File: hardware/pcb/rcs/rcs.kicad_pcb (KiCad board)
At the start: 2 copper layers, 160.5 x 112 mm, 19 parts, among them J1 Conn_01x02_Socket, J2 Conn_01x02_Socket, J3 Conn_01x02_Socket, J4 Conn_01x02_Socket, J5 Conn_01x02_Socket, J6 Conn_01x02_Socket, Q1 BS170, Q2 BS170, Q3 BS170, Q4 BS170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

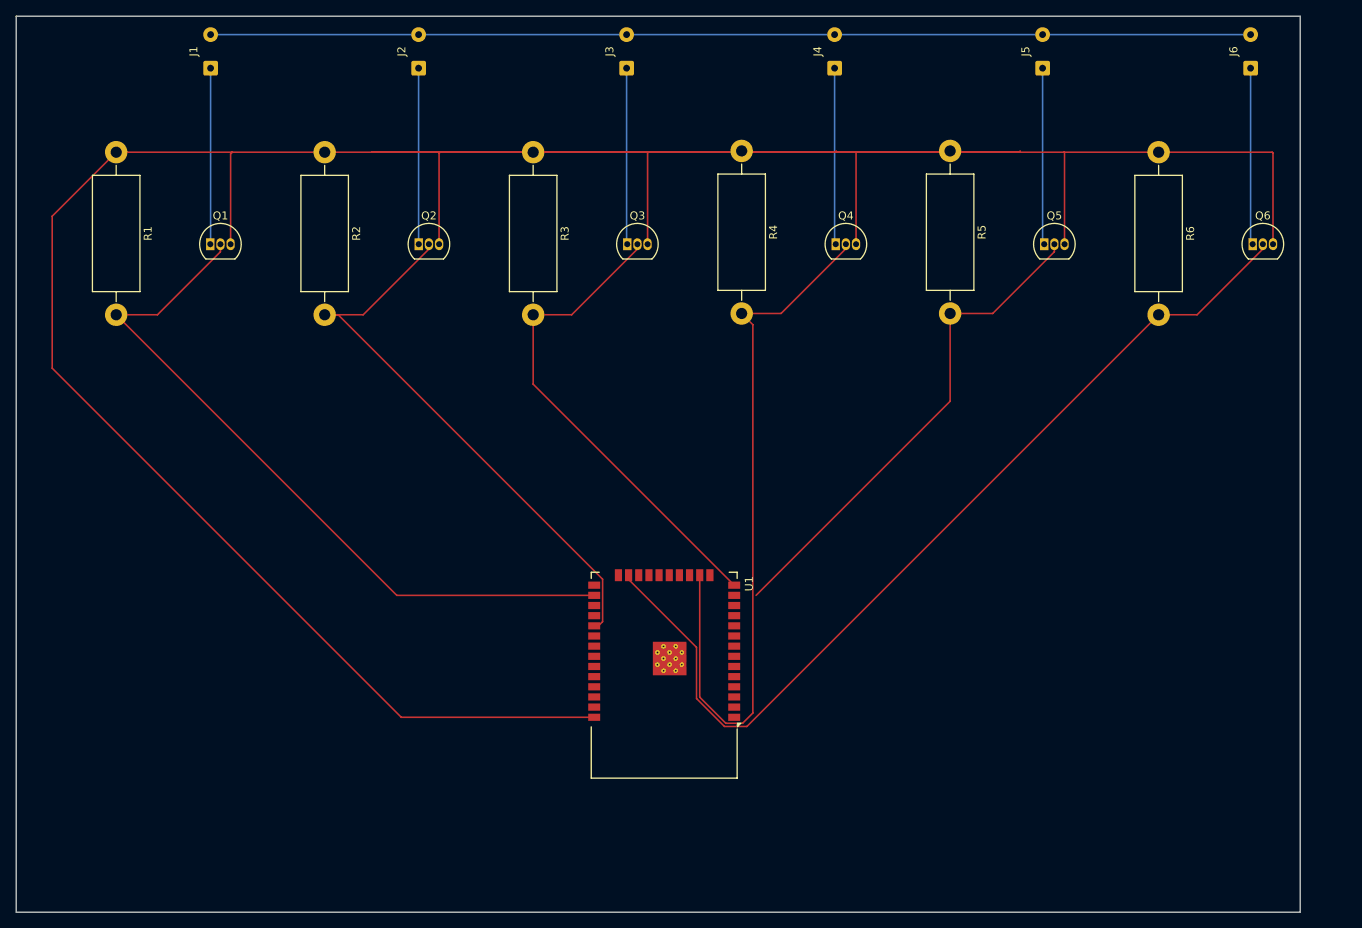
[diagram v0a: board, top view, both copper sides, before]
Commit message: Add ESP32 dev board schematic and footprint, make draft PCB
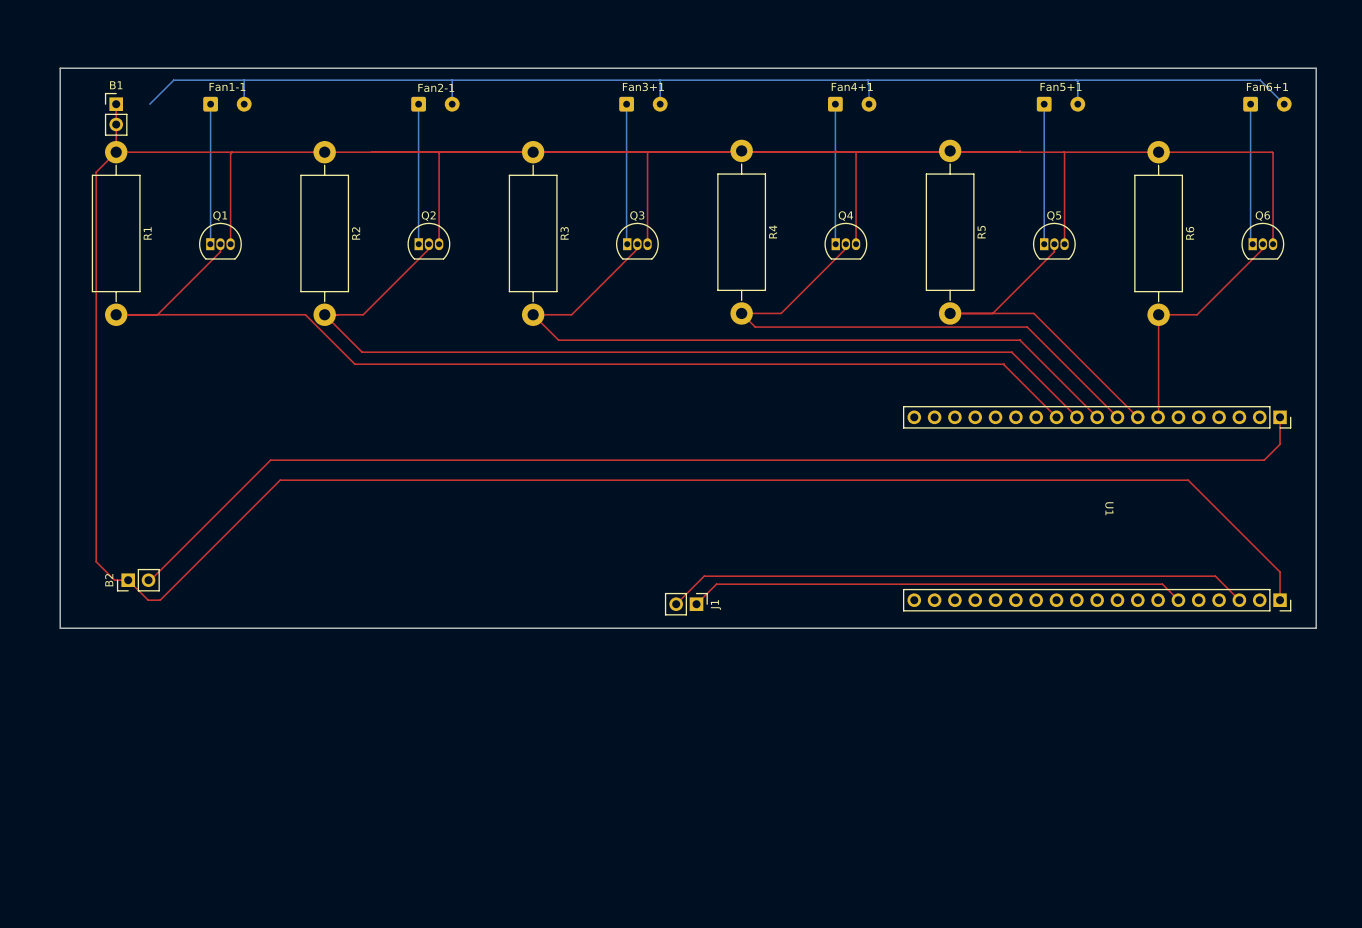
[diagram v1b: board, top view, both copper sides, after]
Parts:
- added B1: 4S, Connector_PinHeader_2.54mm:PinHeader_1x02_P2.54mm_Vertical, F.Cu at (74.0, 24.0)
- added B2: 3V3, Connector_PinHeader_2.54mm:PinHeader_1x02_P2.54mm_Vertical, F.Cu at (75.5, 83.5)
- added J1: UART, Connector_PinHeader_2.54mm:PinHeader_1x02_P2.54mm_Vertical, F.Cu at (146.5, 86.5)
- Fan1-1: renamed from J1; value Conn_01x02_Socket -> Fan1+
- Fan2-1: renamed from J2; value Conn_01x02_Socket -> Fan2+
- Fan3+1: renamed from J3; value Conn_01x02_Socket -> Fan3-
- Fan4+1: renamed from J4; value Conn_01x02_Socket -> Fan4-
- Fan5+1: renamed from J5; value Conn_01x02_Socket -> Fan5-
- Fan6+1: renamed from J6; value Conn_01x02_Socket -> Fan6-
- U1: value ESP32-WROOM-32 -> ESP32; footprint RF_Module:ESP32-WROOM-32 -> custom:ESP32
- moved U1 79.0 mm to (219.5, 74.6), turned to -90 degrees
- moved Fan5+1 4.50 mm to (190.0, 24.0), turned to 0 degrees
- moved Fan4+1 4.50 mm to (163.9, 24.0), turned to 0 degrees
- moved Fan1-1 4.50 mm to (85.8, 24.0), turned to 0 degrees
- moved Fan2-1 4.50 mm to (111.8, 24.0), turned to 0 degrees
- moved Fan3+1 4.50 mm to (137.8, 24.0), turned to 0 degrees
- moved Fan6+1 4.50 mm to (215.8, 24.0), turned to 0 degrees
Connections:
- U1 pad 1: GND -> +3.3V
- U1 pad 10: unconnected-(U1-IO25-Pad10) -> Fan3
- U1 pad 11: unconnected-(U1-IO26-Pad11) -> Fan2
- U1 pad 12: unconnected-(U1-IO27-Pad12) -> Fan1
- U1 pad 13: Fan5 -> unconnected-(U1-P12-Pad13)
- U1 pad 14: Fan3 -> unconnected-(U1-GND-Pad14)
- U1 pad 15: GND -> unconnected-(U1-P13-Pad15)
- U1 pad 16: Fan4 -> unconnected-(U1-SD2-Pad16)
- U1 pad 2: +3.3V -> unconnected-(U1-EN-Pad2)
- U1 pad 20: unconnected-(U1-SCK/CLK-Pad20) -> GND
- U1 pad 22: unconnected-(U1-SDI/SD1-Pad22) -> Net-(J1-Pin_2)
- U1 pad 23: Fan6 -> unconnected-(U1-TX-Pad23)
- U1 pad 25: unconnected-(U1-IO0-Pad25) -> Net-(J1-Pin_1)
- U1 pad 26: Fan1 -> unconnected-(U1-GND-Pad26)
- U1 pad 29: Fan2 -> unconnected-(U1-P18-Pad29)
- U1 pad 38: GND -> unconnected-(U1-CLK-Pad38)
- U1 pad 7: unconnected-(U1-IO35-Pad7) -> Fan6
- U1 pad 8: unconnected-(U1-IO32-Pad8) -> Fan5
- U1 pad 9: unconnected-(U1-IO33-Pad9) -> Fan4
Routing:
- net +3.3V: track 0.00 -> 152.0 mm
- net GND: track 469.1 -> 575.6 mm
- net Fan6: track 116.5 -> 29.9 mm
- net Net-(J1-Pin_2): track 0.00 -> 73.1 mm
- net Net-(J1-Pin_1): track 0.00 -> 62.1 mm
- net Fan1: track 91.5 -> 140.1 mm
- net Fan2: track 72.0 -> 118.1 mm
- net Fan3: track 61.3 -> 92.9 mm
- net +15V: track 130.0 -> 159.4 mm
- net Fan4: track 91.2 -> 69.3 mm
- net Fan5: track 62.5 -> 46.0 mm
- net Net-(Fan6+1-Pin_1): track 22.1 -> 17.6 mm
- net Net-(Fan3+1-Pin_1): track 22.0 -> 17.5 mm
- net Net-(Fan2-1-Pin_1): track 22.0 -> 17.5 mm
- net Net-(Fan1-1-Pin_1): track 22.0 -> 17.5 mm
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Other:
- board size 160.5 x 112 mm -> 157 x 70 mm

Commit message: More compact PCB layout
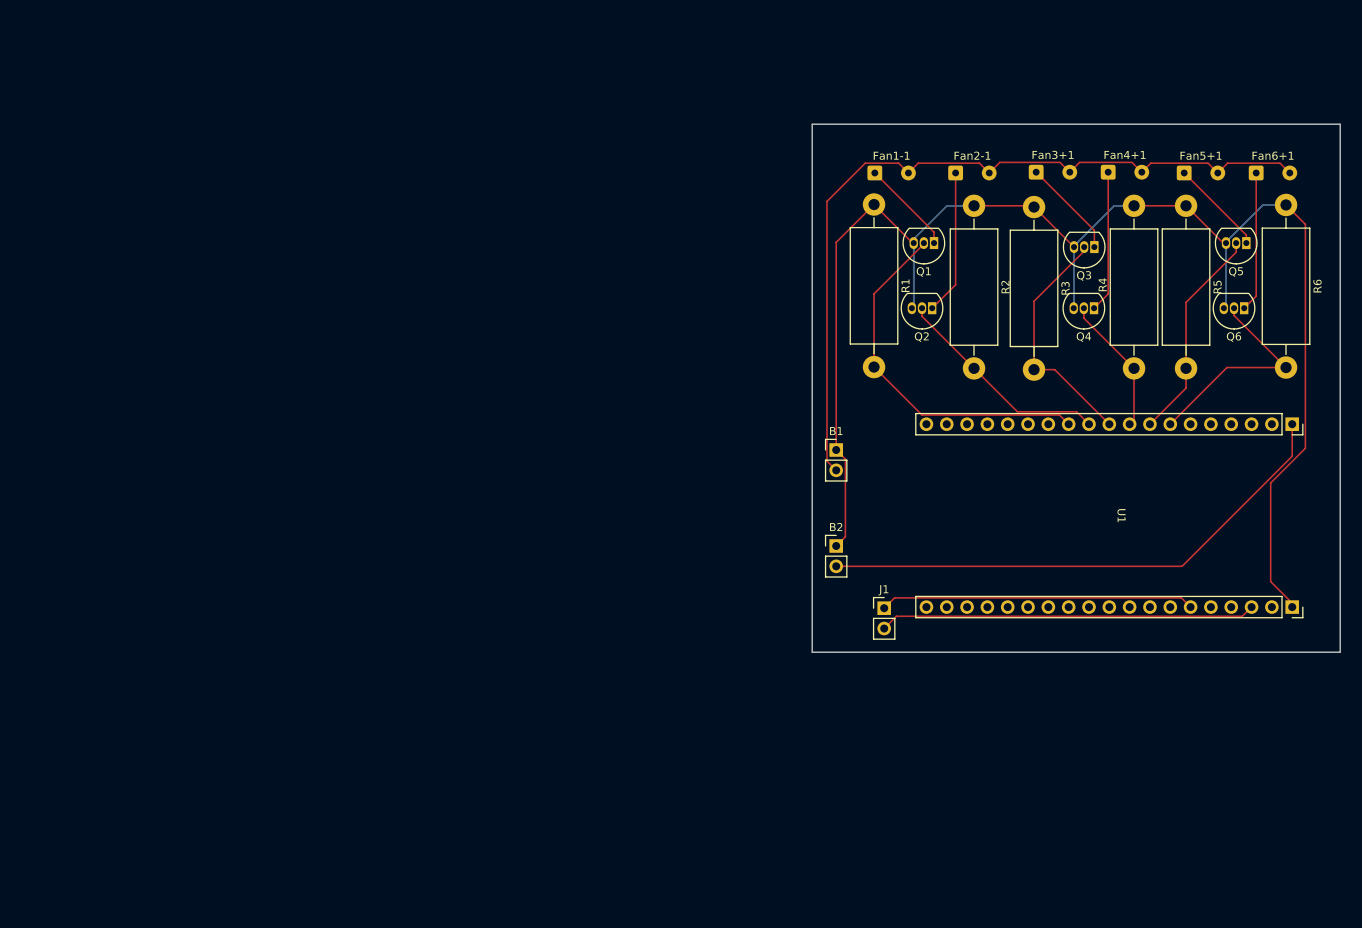
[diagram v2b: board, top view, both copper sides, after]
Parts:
- moved B1 99.8 mm to (164.0, 67.2)
- moved R1 95.0 mm to (168.7, 36.5)
- moved Q1 90.5 mm to (176.2, 41.4), turned to 180 degrees
- moved B2 88.6 mm to (164.0, 79.2), turned to 0 degrees
- moved Fan1-1 83.5 mm to (168.8, 32.6)
- moved R2 81.4 mm to (181.2, 36.7)
- moved Fan2-1 67.7 mm to (178.9, 32.6)
- moved Q2 64.7 mm to (176.0, 49.5), turned to 180 degrees
- moved R3 63.0 mm to (188.7, 36.9)
- moved Q3 58.4 mm to (196.3, 41.9), turned to 180 degrees
- moved Fan3+1 51.9 mm to (189.0, 32.5)
- moved R4 49.5 mm to (201.2, 36.7)
- moved Fan4+1 35.1 mm to (198.0, 32.5)
- moved Q4 33.3 mm to (196.2, 49.5), turned to 180 degrees
- moved R5 30.3 mm to (207.7, 36.7)
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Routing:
- net GND: track 575.6 -> 188.2 mm
- net Fan1: track 140.1 -> 45.9 mm
- net Fan2: track 118.1 -> 28.0 mm
- net +3.3V: track 152.0 -> 66.9 mm
- net Fan3: track 92.9 -> 30.5 mm
- net +15V: track 159.4 -> 99.5 mm
- net Fan4: track 69.3 -> 17.3 mm
- net Net-(J1-Pin_2): track 73.1 -> 47.5 mm
- net Net-(J1-Pin_1): track 62.1 -> 39.8 mm
- net Fan5: track 46.0 -> 26.9 mm
- net Net-(Fan5+1-Pin_1): track 17.8 -> 12.0 mm
- net Net-(Fan1-1-Pin_1): track 17.5 -> 11.8 mm
- net Net-(Fan3+1-Pin_1): track 17.5 -> 12.4 mm
- net Fan6: track 29.9 -> 27.3 mm
- net Net-(Fan2-1-Pin_1): track 17.5 -> 18.1 mm
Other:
- board size 157 x 70 mm -> 66 x 66 mm

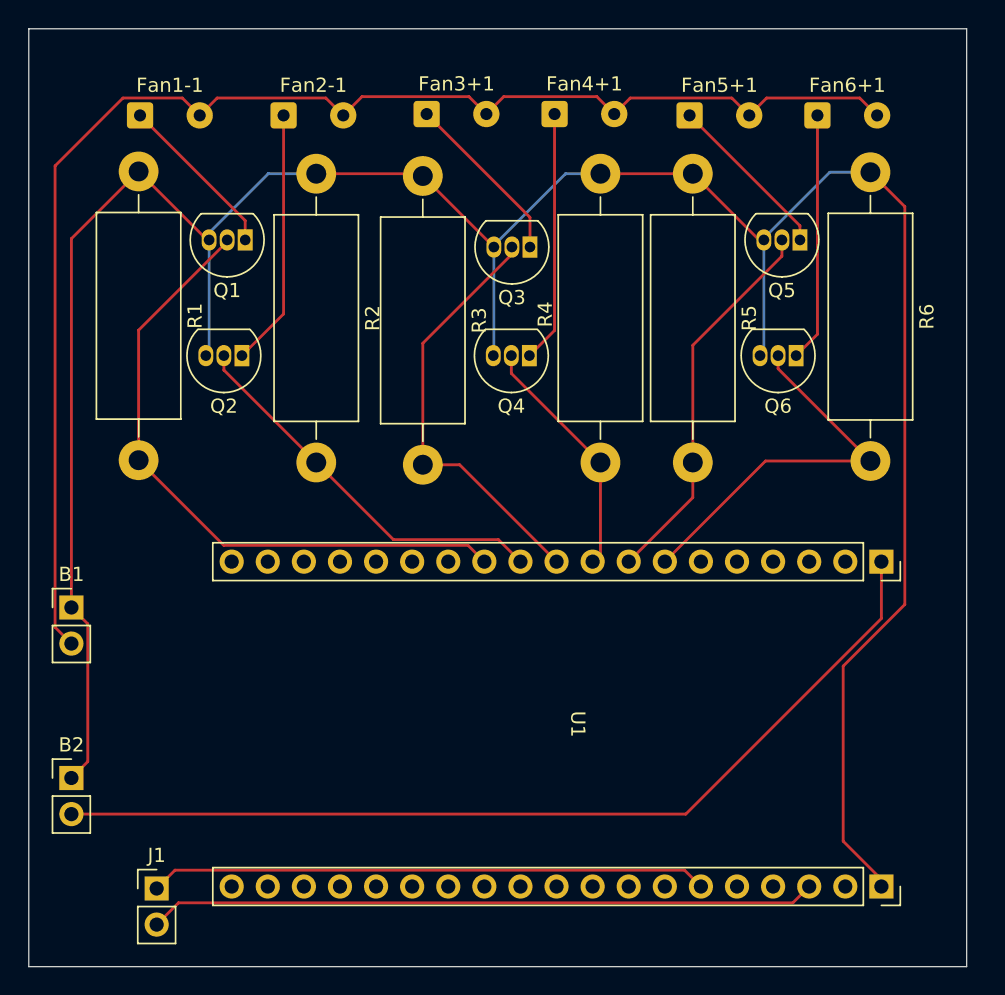
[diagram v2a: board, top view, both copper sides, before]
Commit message: Add minimum trace width and screw holes
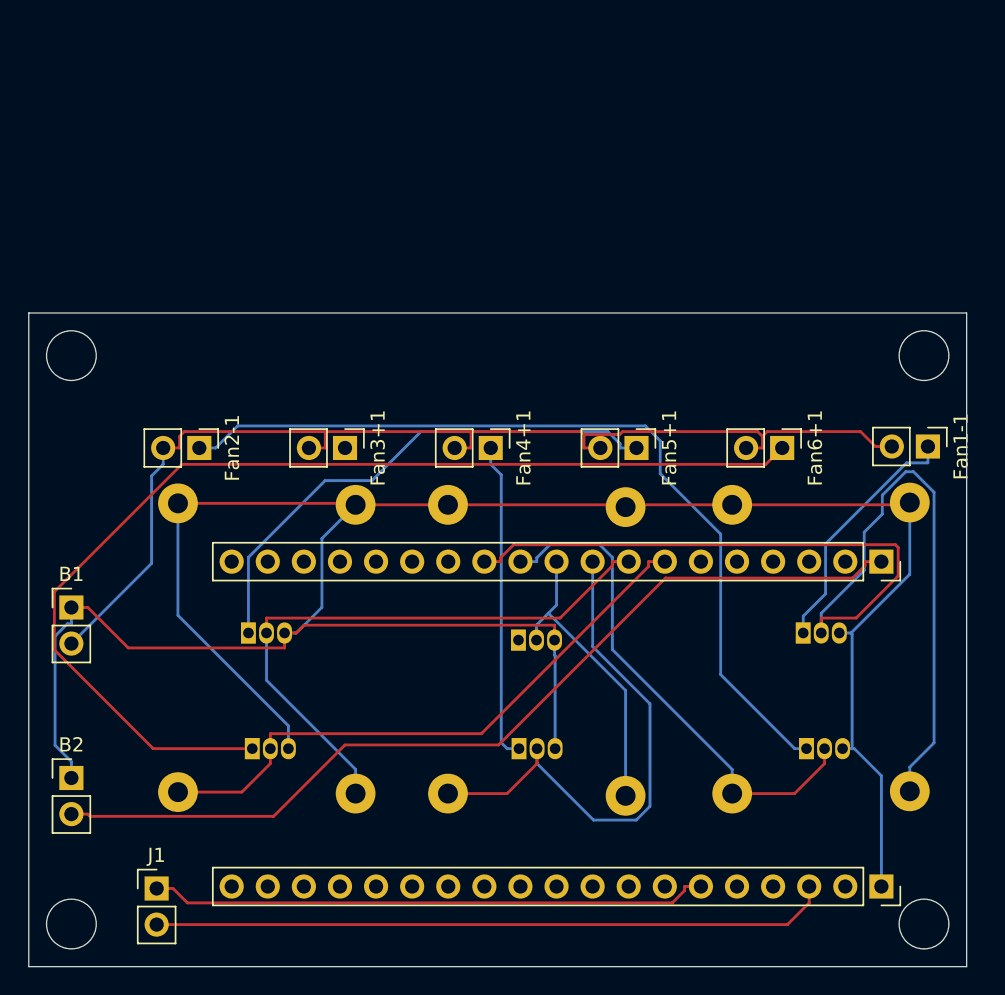
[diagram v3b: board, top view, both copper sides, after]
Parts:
- Fan1-1, Fan2-1, Fan3+1, Fan4+1, Fan5+1, Fan6+1: footprint Connector_Wire:SolderWire-0.25sqmm_1x02_P4.2mm_D0.65mm_OD1.7mm -> Connector_PinHeader_2.54mm:PinHeader_1x02_P2.54mm_Vertical
- Q1, Q2, Q3, Q4, Q5, Q6, R1, R2, R3, R4, R5, R6: moved to B.Cu
- moved Fan1-1 60.1 mm to (224.3, 55.9), turned to -90 degrees
- moved R1 59.1 mm to (223.0, 59.8)
- moved R6 54.0 mm to (171.5, 59.9)
- moved Q2 48.4 mm to (215.7, 77.2), turned to 0 degrees
- moved Q1 48.0 mm to (215.5, 69.0), turned to 0 degrees
- moved Q5 47.7 mm to (176.5, 69.0), turned to 0 degrees
- moved Q6 47.2 mm to (176.7, 77.2), turned to 0 degrees
- moved R2 37.4 mm to (210.5, 60.0)
- moved R5 33.3 mm to (184.0, 60.0)
- moved Q3 27.7 mm to (195.5, 69.5), turned to 0 degrees
- moved Q4 27.7 mm to (195.5, 77.2), turned to 0 degrees
- moved R3 27.3 mm to (203.0, 60.2)
- moved R4 25.7 mm to (190.5, 60.0)
- moved Fan3+1 24.2 mm to (183.3, 56.0), turned to -90 degrees
- moved Fan2-1 24.1 mm to (173.0, 56.0), turned to -90 degrees
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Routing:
- net Net-(Fan6+1-Pin_1): track 17.5 -> 76.3 mm
- net Net-(Fan2-1-Pin_1): track 18.1 -> 59.9 mm
- net Fan1: track 45.9 -> 77.7 mm
- net Net-(Fan5+1-Pin_1): track 12.0 -> 36.9 mm
- net +15V: track 99.5 -> 78.2 mm
- net Fan4: track 17.3 -> 38.1 mm
- net Fan5: track 26.9 -> 42.3 mm
- net Fan6: track 27.3 -> 42.4 mm
- net GND: track 188.2 -> 173.3 mm
- net Net-(Fan3+1-Pin_1): track 12.4 -> 0.00 mm
- net Fan3: track 30.5 -> 21.2 mm
- net Fan2: track 28.0 -> 36.0 mm
- net Net-(Fan1-1-Pin_1): track 11.8 -> 17.6 mm
- net Net-(Fan4+1-Pin_1): track 17.7 -> 22.5 mm
- net +3.3V: track 66.9 -> 64.7 mm
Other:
- board size 66 x 66 mm -> 66 x 46 mm
